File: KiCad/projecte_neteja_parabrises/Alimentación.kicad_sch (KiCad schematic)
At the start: 3 parts, among them U2 LM2596S-5, U3 LM1117DT-3.3

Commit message: botonera
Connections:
- net 5V: now reaches U2.2 (OUT), U3.3 (VI)
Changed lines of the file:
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@@
+		(color 0 0 0 0)
+	)
+	(junction
+		(at 134.62 86.36)
+		(diameter 0)
 		(color 0 0 0 0)
 	)
@@
 		(pts
 			(xy 146.05 93.98) (xy 146.05 95.25)
+		)
+		(stroke
+			(width 0)
+			(type default)
+		)
+	)
+	(wire
+		(pts
+			(xy 134.62 86.36) (xy 134.62 90.17)
 		)
 		(stroke
@@
 	(wire
 		(pts
+			(xy 134.62 86.36) (xy 138.43 86.36)
+		)
+		(stroke
+			(width 0)
+			(type default)
+		)
+	)
+	(wire
+		(pts
 			(xy 153.67 86.36) (xy 162.56 86.36)
 		)
@@
 	(wire
 		(pts
-			(xy 130.81 86.36) (xy 138.43 86.36)
+			(xy 130.81 86.36) (xy 134.62 86.36)
 		)
 		(stroke
@@
 				(hide yes)
 			)
+		)
+	)
+	(global_label "5V"
+		(shape input)
+		(at 134.62 90.17 270)
+		(fields_autoplaced yes)
+		(effects
+			(font
+				(size 1.27 1.27)
+			)
+			(justify right)
+		)
+		(property "Intersheetrefs" "${INTERSHEET_REFS}"
+			(at 134.62 95.4533 90)
+			(effects
+				(font
+					(size 1.27 1.27)
+				)
+				(justify right)
+				(hide yes)
+			)

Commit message: SCH V1
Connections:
- net 12V: now reaches BT1.1 (+), U2.1 (VIN), U2.5 (~{ON}/OFF)
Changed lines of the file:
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@@
+		)
+	)
+	(global_label "12V"
+		(shape input)
+		(at 98.425 81.28 90)
+		(fields_autoplaced yes)
+		(effects
+			(font
+				(size 1.27 1.27)
+			)
+			(justify left)
+		)
+		(property "Intersheetrefs" "${INTERSHEET_REFS}"
+			(at 98.425 74.7872 90)
+			(effects
+				(font
+					(size 1.27 1.27)
+				)
+				(justify left)
+				(hide yes)
+			)
 		)
 	)

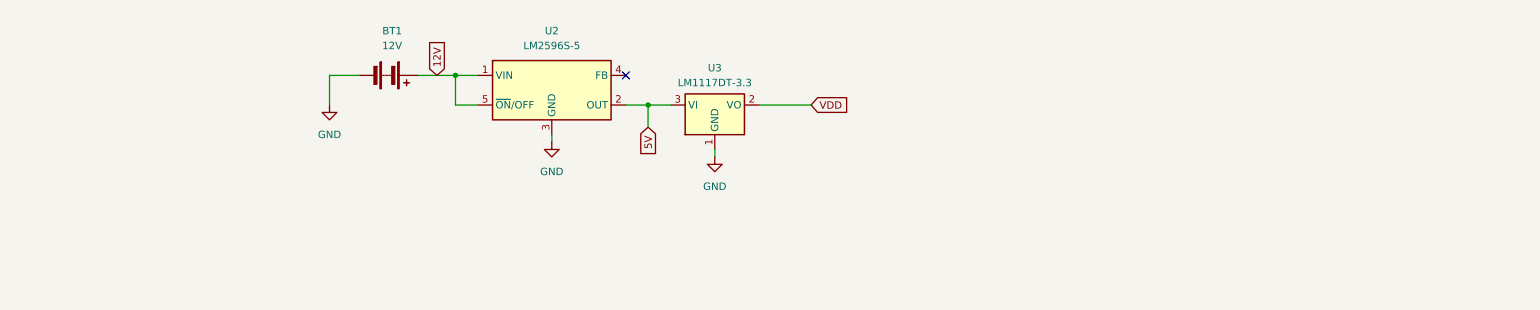
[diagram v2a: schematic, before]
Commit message: alimentacio millora
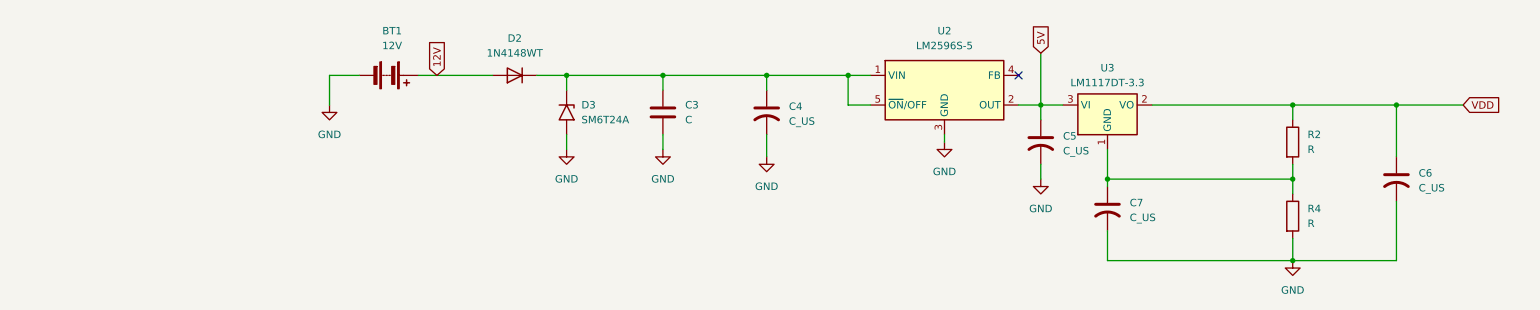
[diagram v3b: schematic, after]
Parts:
- added C3: C, symbol Device:C
- added C4, C5, C6, C7: C_US, symbol Device:C_US
- added D2: 1N4148WT, Diode_SMD:D_SOD-523, symbol Diode:1N4148WT
- added D3: SM6T24A, Diode_SMD:D_SMB, symbol Diode:SM6T24A
- added R2, R4: R, symbol Device:R
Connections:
- net 12V: now also D2.2 (A); no longer U2.1 (VIN), U2.5 (~{ON}/OFF)
- net 5V: now also C5.1
- net GND: now also C3.2, C4.2, C5.2, C6.2, C7.2, D3.2 (A2), R4.2; no longer U3.1 (GND)
- net VDD: now also C6.1, R2.1
- new net: C7.1, R2.2, R4.1, U3.1 (GND)
- new net: C3.1, C4.1, D2.1 (K), D3.1 (A1), U2.1 (VIN), U2.5 (~{ON}/OFF)
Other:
- moved on the sheet: U2, U3

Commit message: alimentacio acabada
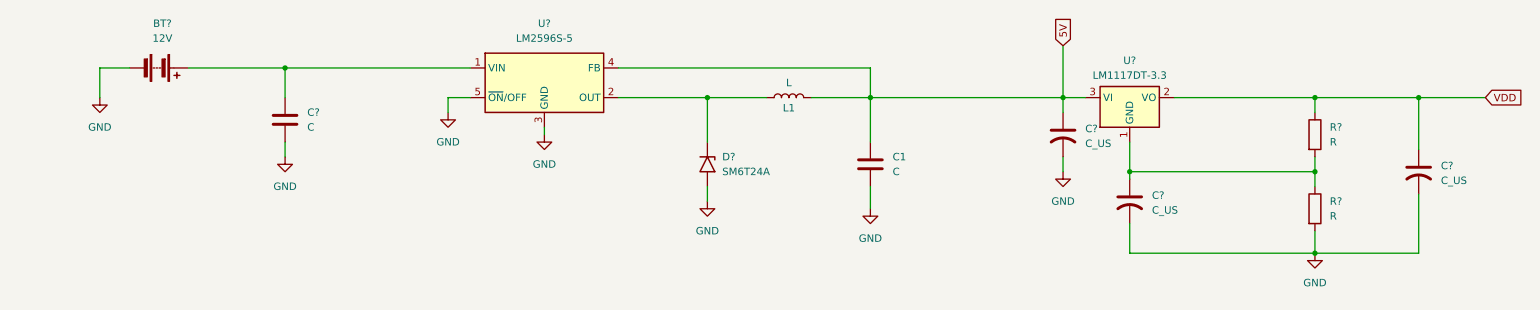
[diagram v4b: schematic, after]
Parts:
- removed C4: C_US, symbol Device:C_US
- removed D2: 1N4148WT, Diode_SMD:D_SOD-523, symbol Diode:1N4148WT
- added C1: C, symbol Device:C
- added L1: L, symbol Device:L
- renumbered BT1 to BT?, C5 to C?, C3 to C?, C6 to C?, C7 to C?, D3 to D?, R4 to R?, R2 to R?, U3 to U?, U2 to U?
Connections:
- net 12V is gone; now on an unnamed net: BT?.1 (+)
- net 5V: now also U?.4 (FB), C1.1, L1.2; no longer U?.2 (OUT)
- net GND: now also U?.5 (~{ON}/OFF), C1.2
- net at C?.1, U?.1 (VIN): no longer D?.1 (A1), U?.5 (~{ON}/OFF)
- new net: D?.1 (A1), L1.1, U?.2 (OUT)
- no-connect marks 1 -> 0
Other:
- moved on the sheet: BT?, C?, D?, R?, U?

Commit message: alimentacio arreglada
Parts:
- C1: value C -> 220uF
- C?: value C_US -> 10uF
- C?: value C -> 680uF
- C?: value C_US -> 100uF
- L1: value L -> 33uH
- R?: value R -> 1k
- R?: value R -> 121
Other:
- moved on the sheet: BT?, C1, C?, D?, L1, R?, U?

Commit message: ESQUEMATICO V2
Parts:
- gave numbers to parts that had none: 10
- renumbered C1 to C12
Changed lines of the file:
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@@
 		(dnp no)
 		(fields_autoplaced yes)
-		(property "Reference" "#PWR?"
+		(property "Reference" "#PWR018"
 			(at 236.22 118.11 0)
 			(effects
@@
 		(dnp no)
 		(fields_autoplaced yes)
-		(property "Reference" "U?"
+		(property "Reference" "U3"
 			(at 204.47 78.74 0)
 			(effects
@@
 		(dnp no)
 		(fields_autoplaced yes)
-		(property "Reference" "R?"
+		(property "Reference" "R4"
 			(at 238.76 102.8699 0)
 			(effects
@@
 		(dnp no)
 		(fields_autoplaced yes)
-		(property "Reference" "C?"
+		(property "Reference" "C13"
 			(at 193.04 90.4239 0)
 			(effects
@@
 			(project ""
 				(path "/83fe8808-b70b-463e-9fcd-89556c9690a9/a8962c48-b3a9-4541-b459-e1566624b900"
-					(reference "C5")
+					(reference "C13")
 					(unit 1)
 				)
@@
 		(dnp no)
 		(fields_autoplaced yes)
-		(property "Reference" "#PWR02"
+		(property "Reference" "#PWR?"
 			(at 160.02 110.49 0)
 			(effects
@@
 				)
 			)
+			(project "projecte_neteja_parabrises"
+				(path "/83fe8808-b70b-463e-9fcd-89556c9690a9/a8962c48-b3a9-4541-b459-e1566624b900"
+					(reference "#PWR?")
+					(unit 1)
+				)
+			)
 		)
 	)
@@
 		(dnp no)
 		(fields_autoplaced yes)
-		(property "Reference" "#PWR01"
+		(property "Reference" "#PWR?"
 			(at 87.63 93.98 0)
 			(effects
@@
 				)
 			)
+			(project "projecte_neteja_parabrises"
+				(path "/83fe8808-b70b-463e-9fcd-89556c9690a9/a8962c48-b3a9-4541-b459-e1566624b900"
+					(reference "#PWR?")
+					(unit 1)
+				)
+			)
 		)
 	)
@@
 		(dnp no)
 		(fields_autoplaced yes)
-		(property "Reference" "#PWR?"
+		(property "Reference" "#PWR017"
 			(at 189.23 104.14 0)
 			(effects
@@
 		(dnp no)
 		(fields_autoplaced yes)
-		(property "Reference" "#PWR?"
+		(property "Reference" "#PWR015"
 			(at 59.69 101.6 0)
 			(effects
@@
 		(dnp no)
 		(fields_autoplaced yes)
-		(property "Reference" "#PWR?"
+		(property "Reference" "#PWR014"
 			(at 132.08 109.22 0)
 			(effects
@@
 		(dnp no)
 		(fields_autoplaced yes)
-		(property "Reference" "C1"
+		(property "Reference" "C12"
 			(at 163.83 95.2499 0)
 			(effects
@@
 				)
 			)
+			(project "projecte_neteja_parabrises"
+				(path "/83fe8808-b70b-463e-9fcd-89556c9690a9/a8962c48-b3a9-4541-b459-e1566624b900"
+					(reference "C12")
+					(unit 1)
+				)
+			)
 		)
 	)
@@
 		(dnp no)
 		(fields_autoplaced yes)
-		(property "Reference" "BT?"
+		(property "Reference" "BT1"
 			(at 38.6715 72.39 90)
 			(effects
@@
 		(dnp no)
 		(fields_autoplaced yes)
-		(property "Reference" "C?"
+		(property "Reference" "C11"
 			(at 63.5 87.6299 0)
 			(effects
@@
 			(project ""
 				(path "/83fe8808-b70b-463e-9fcd-89556c9690a9/a8962c48-b3a9-4541-b459-e1566624b900"
-					(reference "C3")
+					(reference "C11")
 					(unit 1)
 				)
@@
 		(dnp no)
 		(fields_autoplaced yes)
-		(property "Reference" "R?"
+		(property "Reference" "R2"
 			(at 238.76 90.1699 0)
 			(effects
@@
 		(dnp no)
 		(fields_autoplaced yes)
-		(property "Reference" "U?"
+		(property "Reference" "U2"
 			(at 104.14 72.39 0)
 			(effects
@@
 		(dnp no)
 		(fields_autoplaced yes)
-		(property "Reference" "#PWR?"
+		(property "Reference" "#PWR02"
 			(at 104.14 97.79 0)
 			(effects
@@
 		(dnp no)
 		(fields_autoplaced yes)
-		(property "Reference" "#PWR?"
+		(property "Reference" "#PWR01"
 			(at 27.94 91.44 0)
 			(effects
@@
 		(dnp no)
 		(fields_autoplaced yes)
-		(property "Reference" "C?"
+		(property "Reference" "C15"
 			(at 257.81 96.7739 0)
 			(effects
@@
 			(project ""
 				(path "/83fe8808-b70b-463e-9fcd-89556c9690a9/a8962c48-b3a9-4541-b459-e1566624b900"
-					(reference "C6")
+					(reference "C15")
 					(unit 1)
 				)
@@
 		(on_board yes)
 		(dnp no)
-		(property "Reference" "L1"
+		(property "Reference" "L?"
 			(at 146.05 82.804 90)
 			(effects
@@
 				)
 			)
+			(project "projecte_neteja_parabrises"
+				(path "/83fe8808-b70b-463e-9fcd-89556c9690a9/a8962c48-b3a9-4541-b459-e1566624b900"
+					(reference "L?")
+					(unit 1)
+				)
+			)
 		)
 	)
@@
 		(dnp no)
 		(fields_autoplaced yes)
-		(property "Reference" "D?"
+		(property "Reference" "D3"
 			(at 134.62 95.2499 90)
 			(effects
@@
 		(dnp no)
 		(fields_autoplaced yes)
-		(property "Reference" "C?"
+		(property "Reference" "C14"
 			(at 208.28 101.8539 0)
 			(effects
@@
 			(project ""
 				(path "/83fe8808-b70b-463e-9fcd-89556c9690a9/a8962c48-b3a9-4541-b459-e1566624b900"
-					(reference "C7")
-					(unit 1)
-				)
+					(reference "C14")
+					(unit 1)
+				)

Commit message: Error de nombres solucionado
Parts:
- renumbered R2 to R5, R4 to R6, U3 to U1
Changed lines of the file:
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@@
 		(dnp no)
 		(fields_autoplaced yes)
-		(property "Reference" "U3"
+		(property "Reference" "U1"
 			(at 204.47 78.74 0)
 			(effects
@@
 			(project ""
 				(path "/83fe8808-b70b-463e-9fcd-89556c9690a9/a8962c48-b3a9-4541-b459-e1566624b900"
-					(reference "U3")
+					(reference "U1")
 					(unit 1)
 				)
@@
 		(dnp no)
 		(fields_autoplaced yes)
-		(property "Reference" "R4"
+		(property "Reference" "R6"
 			(at 238.76 102.8699 0)
 			(effects
@@
 			(project ""
 				(path "/83fe8808-b70b-463e-9fcd-89556c9690a9/a8962c48-b3a9-4541-b459-e1566624b900"
-					(reference "R4")
+					(reference "R6")
 					(unit 1)
 				)
@@
 		(dnp no)
 		(fields_autoplaced yes)
-		(property "Reference" "#PWR?"
+		(property "Reference" "#PWR0105"
 			(at 160.02 110.49 0)
 			(effects
@@
 			(project "projecte_neteja_parabrises"
 				(path "/83fe8808-b70b-463e-9fcd-89556c9690a9/a8962c48-b3a9-4541-b459-e1566624b900"
-					(reference "#PWR?")
+					(reference "#PWR0105")
 					(unit 1)
 				)
@@
 		(dnp no)
 		(fields_autoplaced yes)
-		(property "Reference" "#PWR?"
+		(property "Reference" "#PWR0104"
 			(at 87.63 93.98 0)
 			(effects
@@
 			(project "projecte_neteja_parabrises"
 				(path "/83fe8808-b70b-463e-9fcd-89556c9690a9/a8962c48-b3a9-4541-b459-e1566624b900"
-					(reference "#PWR?")
+					(reference "#PWR0104")
 					(unit 1)
 				)
@@
 		(dnp no)
 		(fields_autoplaced yes)
-		(property "Reference" "R2"
+		(property "Reference" "R5"
 			(at 238.76 90.1699 0)
 			(effects
@@
 			(project ""
 				(path "/83fe8808-b70b-463e-9fcd-89556c9690a9/a8962c48-b3a9-4541-b459-e1566624b900"
-					(reference "R2")
+					(reference "R5")
 					(unit 1)
 				)
@@
 		(on_board yes)
 		(dnp no)
-		(property "Reference" "L?"
+		(property "Reference" "L1"
 			(at 146.05 82.804 90)
 			(effects
@@
 			(project "projecte_neteja_parabrises"
 				(path "/83fe8808-b70b-463e-9fcd-89556c9690a9/a8962c48-b3a9-4541-b459-e1566624b900"
-					(reference "L?")
-					(unit 1)
-				)
+					(reference "L1")
+					(unit 1)
+				)

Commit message: huellas
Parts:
- C11, C12, C13, C14, C15: footprint (none) -> Capacitor_SMD:C_0805_2012Metric
- R5, R6: footprint (none) -> Resistor_SMD:R_0603_1608Metric_Pad0.98x0.95mm_HandSolder
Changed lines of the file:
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@@
 			)
 		)
-		(property "Footprint" ""
+		(property "Footprint" "Resistor_SMD:R_0603_1608Metric_Pad0.98x0.95mm_HandSolder"
 			(at 234.442 104.14 90)
 			(effects
@@
 			)
 		)
-		(property "Footprint" ""
+		(property "Footprint" "Capacitor_SMD:C_0805_2012Metric"
 			(at 189.23 91.44 0)
 			(effects
@@
 			)
 		)
-		(property "Footprint" ""
+		(property "Footprint" "Capacitor_SMD:C_0805_2012Metric"
 			(at 160.9852 100.33 0)
 			(effects
@@
 			)
 		)
-		(property "Footprint" ""
+		(property "Footprint" "Capacitor_SMD:C_0805_2012Metric"
 			(at 60.6552 92.71 0)
 			(effects
@@
 			)
 		)
-		(property "Footprint" ""
+		(property "Footprint" "Resistor_SMD:R_0603_1608Metric_Pad0.98x0.95mm_HandSolder"
 			(at 234.442 91.44 90)
 			(effects
@@
 			)
 		)
-		(property "Footprint" ""
+		(property "Footprint" "Capacitor_SMD:C_0805_2012Metric"
 			(at 254 97.79 0)
 			(effects
@@
 			)
 		)
-		(property "Footprint" ""
+		(property "Footprint" "Capacitor_SMD:C_0805_2012Metric"
 			(at 204.47 102.87 0)
 			(effects
